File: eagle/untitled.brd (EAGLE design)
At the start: 50 x 50 mm, 46 parts, among them J1 JTAG, Q1 16MHz, U1 MMA3202KEG

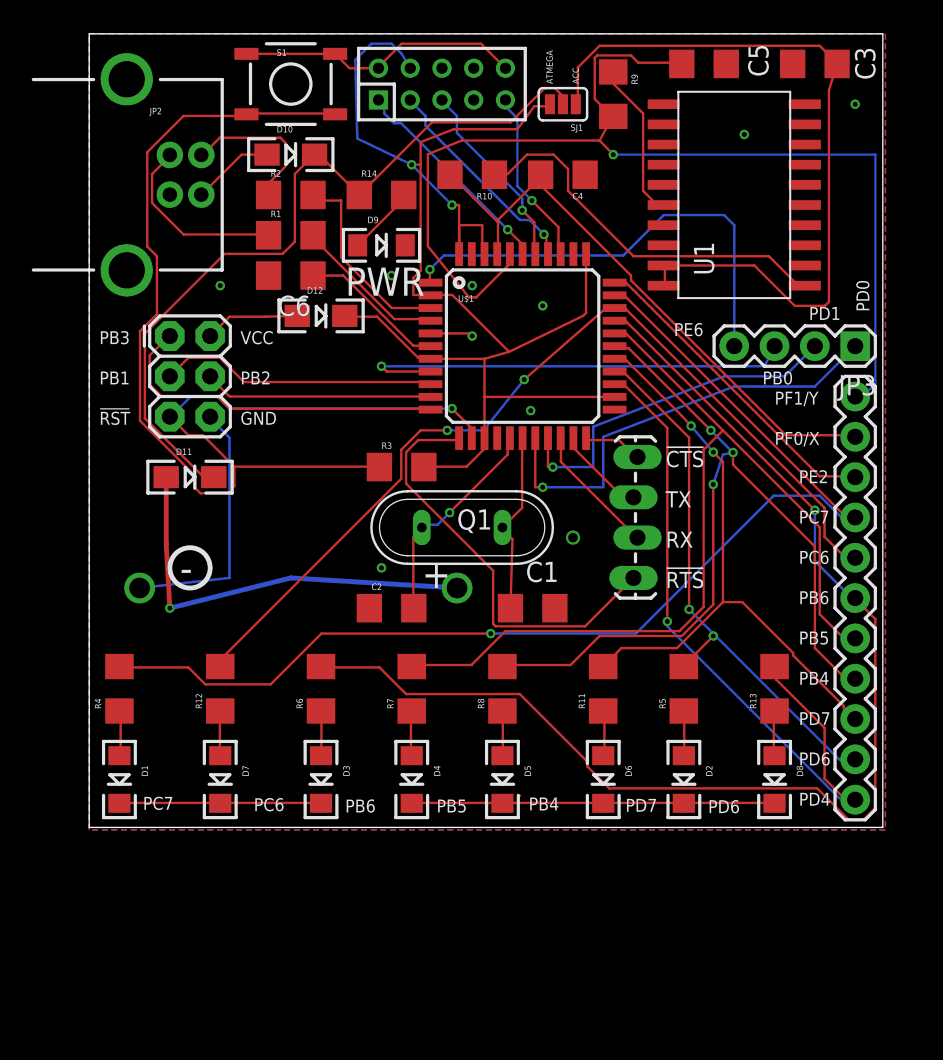
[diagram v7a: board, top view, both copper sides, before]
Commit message: Add BOOT button and reroute stuffs.
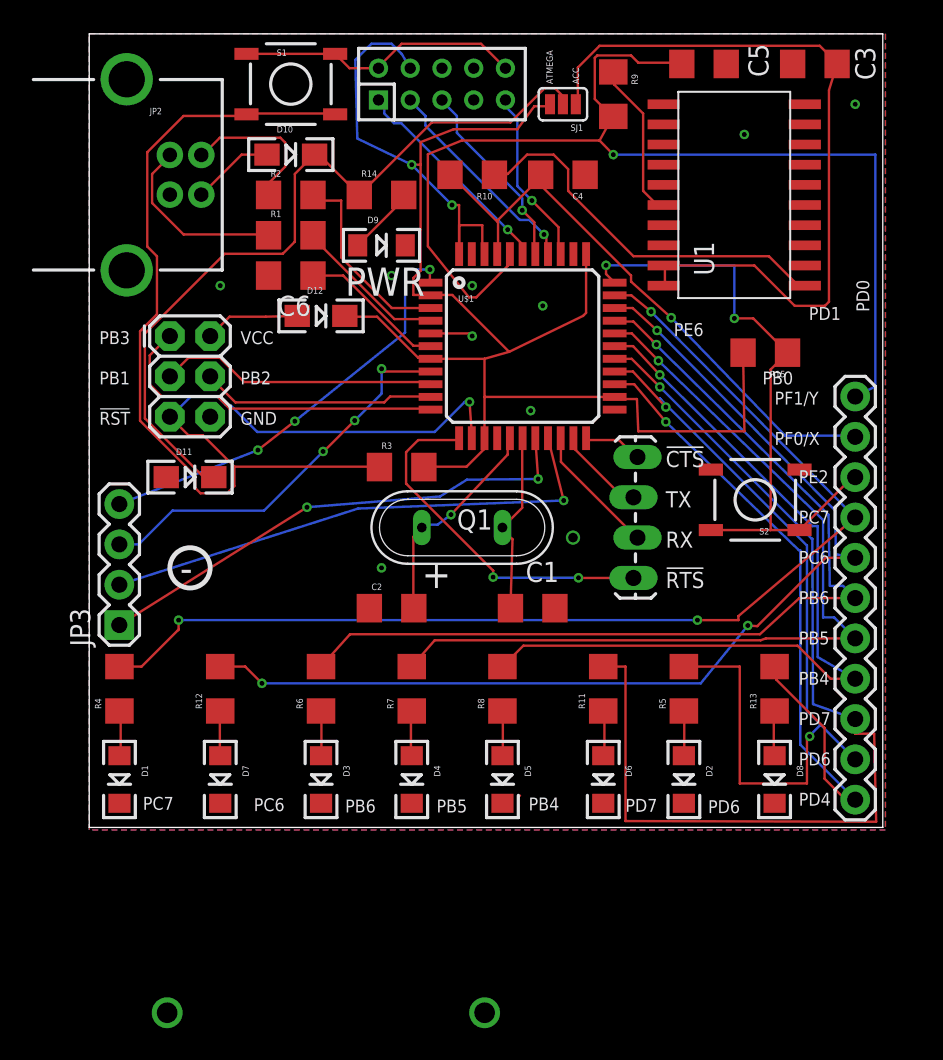
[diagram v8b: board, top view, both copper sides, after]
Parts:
- added R15: 10k, SparkFun-Passives:1206
- added S2: BOOT, SparkFun-Retired:TACTILE-SWITCH-SMD
- moved JP3 49.6 mm to (1.90, 42.8), turned to 90 degrees
- moved G1 26.8 mm to (16.8, 18.3)
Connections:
- net GND-ISO: now also S2.3
- net PE2: now also R15.1, S2.1, S2.2
- net VCC1: now also R15.2
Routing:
- net GND-ISO: track 72.9 -> 21.2 mm
- net N$33: track 26.6 -> 0.00 mm, vias 1 -> 0
- net PD7: track 39.6 -> 65.0 mm, vias 2 -> 1
- net PE2: track 20.2 -> 39.1 mm, vias 0 -> 2
- net PD6: track 34.4 -> 51.9 mm
- net PB6: track 77.5 -> 61.0 mm
- net VCC1: track 91.7 -> 107.4 mm
- net PD1: track 22.6 -> 32.8 mm
- net PC6: track 58.3 -> 67.1 mm, vias 2 -> 3
- net PB7: track 27.0 -> 22.7 mm, vias 0 -> 2
- net PB0: track 28.8 -> 25.2 mm, vias 1 -> 3
- net PD0: track 28.1 -> 31.4 mm, vias 1 -> 2
- net PB5: track 57.9 -> 55.3 mm, vias 0 -> 1
- net N$17: track 75.8 -> 78.2 mm
- net PC7: track 73.3 -> 71.4 mm, vias 1 -> 3
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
